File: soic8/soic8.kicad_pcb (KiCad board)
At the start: 2 copper layers, 15.7 x 10.7 mm, 3 parts, among them J1 Conn_01x04_Male, J2 Conn_01x04_Male, U1 ATSHA204_SOIC8

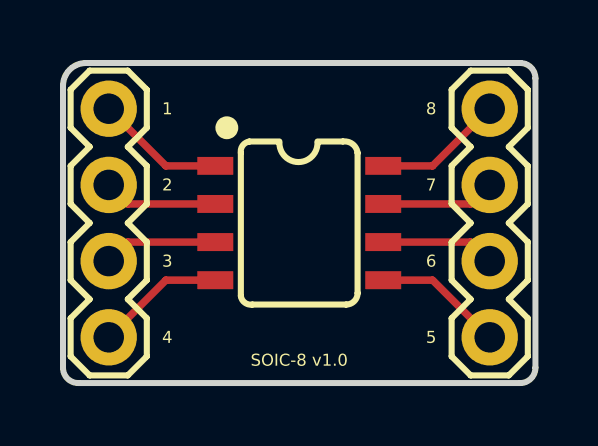
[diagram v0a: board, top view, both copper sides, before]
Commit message: Updated soic-8 with lib
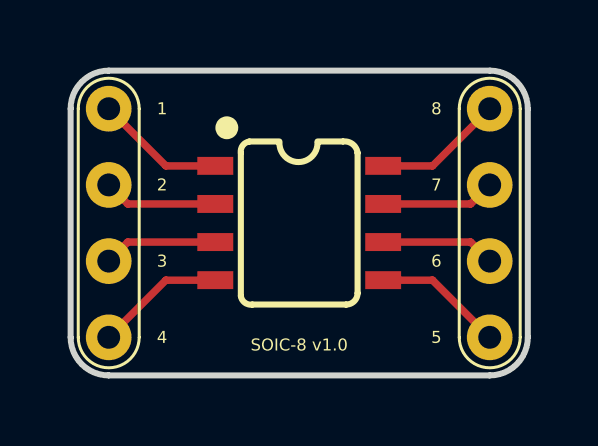
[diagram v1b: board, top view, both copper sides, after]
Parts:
- removed J1, J2: Conn_01x04_Male, Connectors:1X04
- added J3: Conn_01x08_Male, DevPc:bb_2x4, F.Cu at (116.8, 78.7)
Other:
- board size 15.7 x 10.7 mm -> 15.2 x 10.2 mm
- board text removed: "1"
- board text removed: "2"
- board text removed: "3"
- board text removed: "4"
- board text removed: "5"
- board text removed: "6"
- board text removed: "7"
- board text removed: "8"

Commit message: Implemented library footprints on soic-8
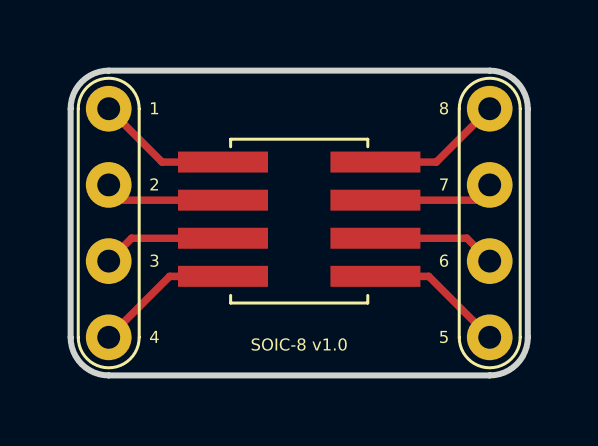
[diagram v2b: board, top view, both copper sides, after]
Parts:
- removed J3: Conn_01x08_Male, DevPc:bb_2x4
- added J1: bb2x4, DevPc:bb_2x4, F.Cu at (116.8, 78.7)
- U1: value ATSHA204_SOIC8 -> u2x4; footprint Silicon-Standard:SO08 -> DevPc:soic-8
- moved U1 3.30 mm to (123.2, 79.2), turned to 0 degrees
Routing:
- net Net-(J1-Pad5): track 4.09 -> 4.65 mm
